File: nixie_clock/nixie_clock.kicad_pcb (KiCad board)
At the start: 2 copper layers, 147.3 x 92.7 mm, 52 parts, among them P1 CONN_01X04, P10 CONN_01X03, P11 CONN_01X02, P12 CONN_01X03, P13 CONN_01X02, P2 CONN_01X03, P3 CONN_01X02, P4 CONN_01X03, P5 CONN_01X02, P6 CONN_01X03, P7 CONN_01X02, P8 CONN_01X03, P9 CONN_01X02, U1 4518, U10 K155ID1, U11 IN-12, U12 4518, U13 4011, U14 K155ID1, U15 IN-12, U16 K155ID1, U17 IN-12, U2 4011, U3 K155ID1, U4 IN-12, U5 K155ID1, U6 IN-12, U7 4518, U8 K155ID1, U9 IN-12

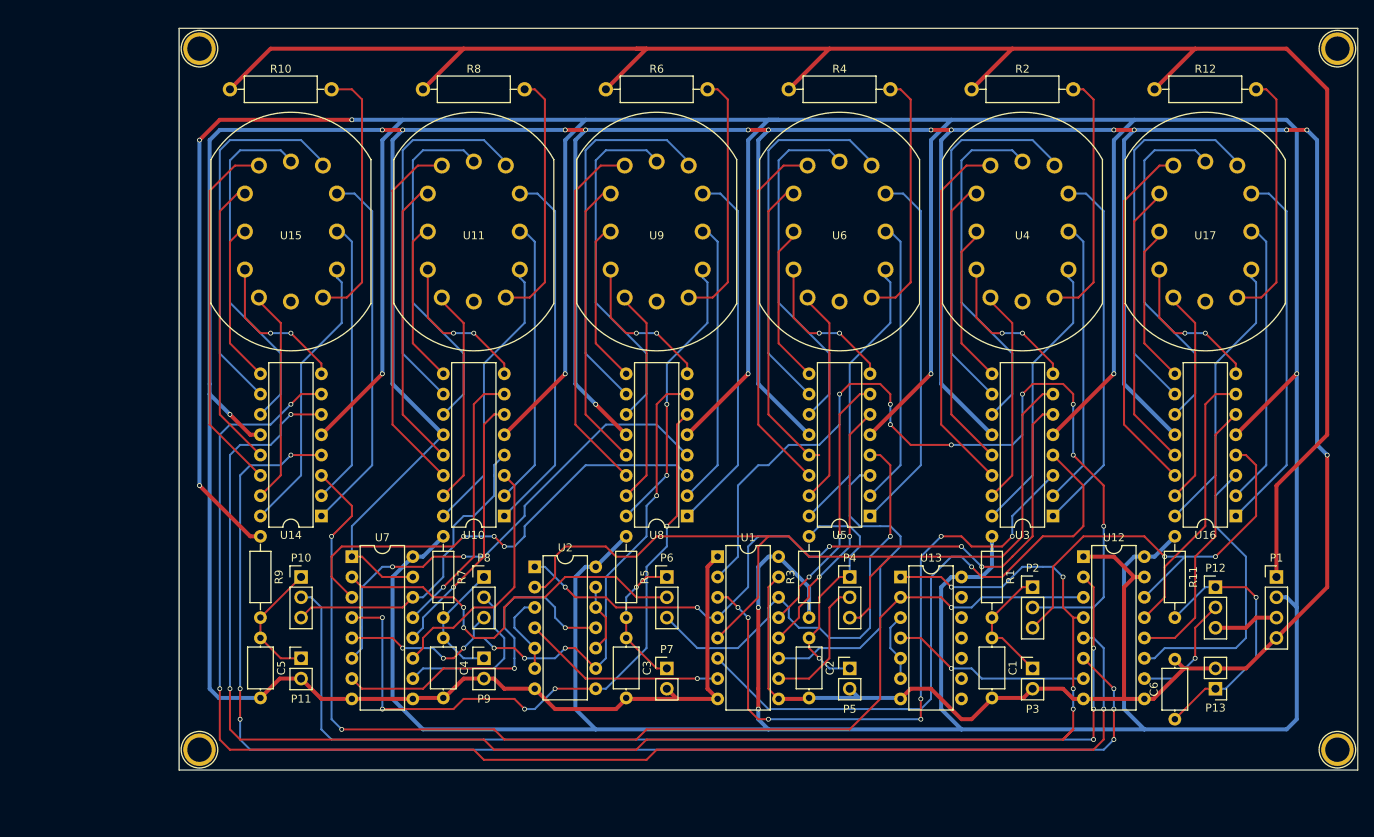
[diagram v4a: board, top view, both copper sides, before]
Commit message: Overhaul of clock board. Fixed hour digits, added more noise immunity, reduced height
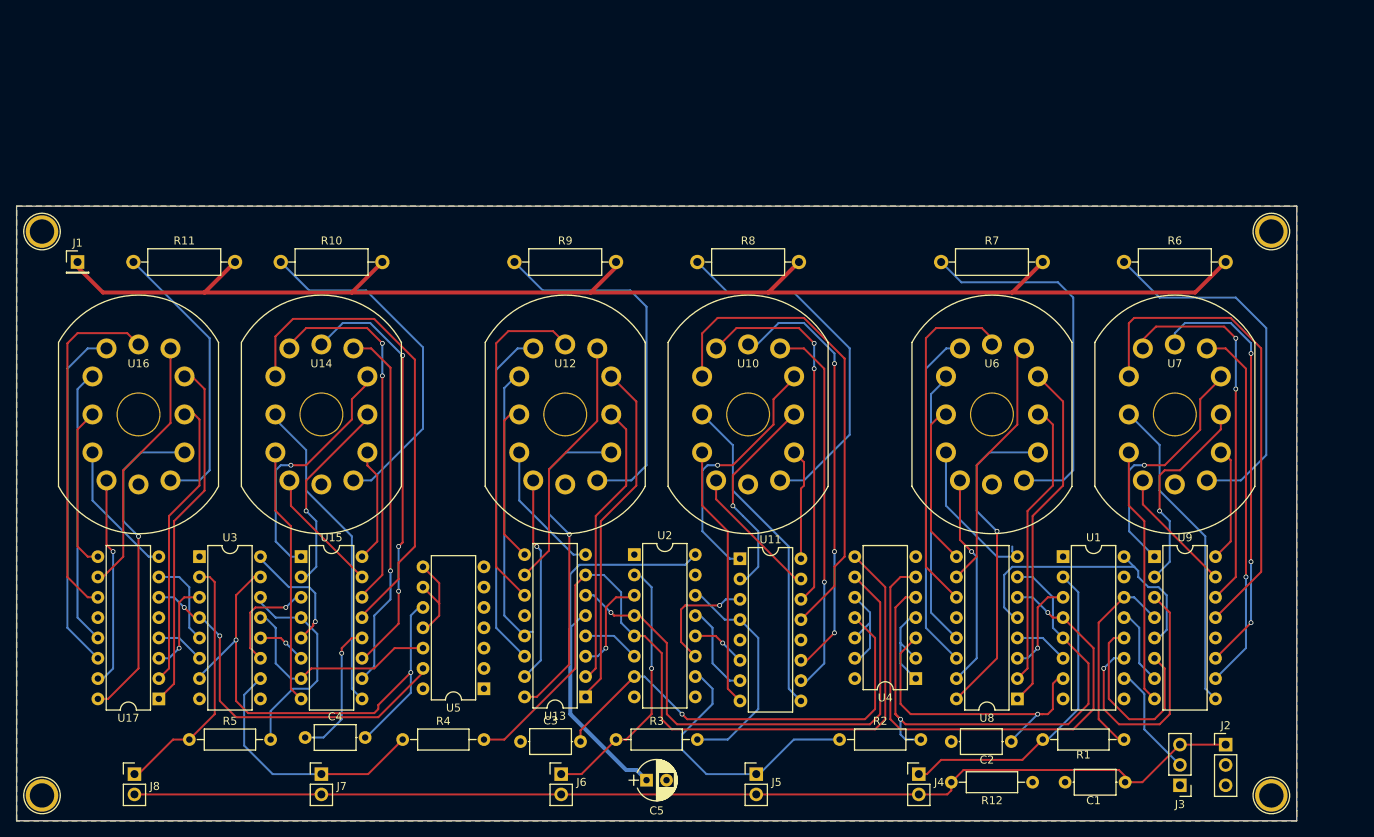
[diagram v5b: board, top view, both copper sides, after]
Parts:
- removed C6: 0.1uF, Capacitors_THT:C_Axial_L5.1mm_D3.1mm_P7.50mm_Horizontal
- removed P1: CONN_01X04, Pin_Headers:Pin_Header_Straight_1x04_Pitch2.54mm
- removed P10, P12, P2, P4, P6, P8: CONN_01X03, Pin_Headers:Pin_Header_Straight_1x03_Pitch2.54mm
- removed P11, P13, P3, P5, P7, P9: CONN_01X02, Pin_Headers:Pin_Header_Straight_1x02_Pitch2.54mm
- removed the REF** at (78.7, 24.1)
- removed the REF** at (221.0, 24.1)
- removed the REF** at (221.0, 111.8)
- removed the REF** at (78.7, 111.8)
- added J1: CONN_01X01, Pin_Headers:Pin_Header_Straight_1x01_Pitch2.54mm, F.Cu at (63.5, 50.8)
- added J2: CONN_01X03, Pin_Headers:Pin_Header_Straight_1x03_Pitch2.54mm, F.Cu at (207.0, 111.1)
- added J3: CONN_01X03, Pin_Headers:Pin_Header_Straight_1x03_Pitch2.54mm, F.Cu at (201.3, 116.2)
- added J4: CONN_01X02, Pin_Headers:Pin_Header_Straight_1x02_Pitch2.54mm, F.Cu at (168.7, 114.8)
- added J5: CONN_01X02, Pin_Headers:Pin_Header_Straight_1x02_Pitch2.54mm, F.Cu at (148.3, 114.8)
- added J6: CONN_01X02, Pin_Headers:Pin_Header_Straight_1x02_Pitch2.54mm, F.Cu at (124.0, 114.8)
- added J7: CONN_01X02, Pin_Headers:Pin_Header_Straight_1x02_Pitch2.54mm, F.Cu at (94.0, 114.8)
- added J8: CONN_01X02, Pin_Headers:Pin_Header_Straight_1x02_Pitch2.54mm, F.Cu at (70.6, 114.8)
- added REF**: 1pin, Connectors:1pin, F.Cu at (59.1, 47.0)
- added REF**: 1pin, Connectors:1pin, F.Cu at (212.7, 47.0)
- added REF**: 1pin, Connectors:1pin, F.Cu at (59.1, 117.5)
- added REF**: 1pin, Connectors:1pin, F.Cu at (212.7, 117.5)
- C5: value 0.1uF -> 10uF; footprint Capacitors_THT:C_Axial_L5.1mm_D3.1mm_P7.50mm_Horizontal -> Capacitors_THT:CP_Radial_D5.0mm_P2.50mm
- R11, R7, R9: value 1K -> 33K; footprint Resistors_THT:R_Axial_DIN0207_L6.3mm_D2.5mm_P10.16mm_Horizontal -> hv:R_Axial_DIN0309_L9.0mm_D3.2mm_P12.70mm_Horizontal_Thick
- R12: value 33K -> 4.7K; footprint hv:R_Axial_DIN0309_L9.0mm_D3.2mm_P12.70mm_Horizontal_Thick -> Resistors_THT:R_Axial_DIN0207_L6.3mm_D2.5mm_P10.16mm_Horizontal
- R2, R4: value 33K -> 1K; footprint hv:R_Axial_DIN0309_L9.0mm_D3.2mm_P12.70mm_Horizontal_Thick -> Resistors_THT:R_Axial_DIN0207_L6.3mm_D2.5mm_P10.16mm_Horizontal
- U10, U14, U16: value K155ID1 -> IN-12; footprint Housings_DIP:DIP-16_W7.62mm -> hv:IN12
- U11, U15, U17, U9: value IN-12 -> K155ID1; footprint hv:IN12 -> Housings_DIP:DIP-16_W7.62mm
- U12, U7: value 4518 -> IN-12; footprint Housings_DIP:DIP-16_W7.62mm -> hv:IN12
- U13: value 4011 -> K155ID1; footprint Housings_DIP:DIP-14_W7.62mm -> Housings_DIP:DIP-16_W7.62mm
- U2: value 4011 -> 4518; footprint Housings_DIP:DIP-14_W7.62mm -> Housings_DIP:DIP-16_W7.62mm
- U3: value K155ID1 -> 4518
- U4: value IN-12 -> 4011; footprint hv:IN12 -> Housings_DIP:DIP-14_W7.62mm
- U5: value K155ID1 -> 4011; footprint Housings_DIP:DIP-16_W7.62mm -> Housings_DIP:DIP-14_W7.62mm
- moved U17 143.3 mm to (73.7, 105.4), turned to 180 degrees
- moved U16 137.7 mm to (71.1, 69.8), turned to 0 degrees
- moved R11 134.6 mm to (70.5, 50.8), turned to 0 degrees
- moved U3 106.8 mm to (78.7, 87.6), turned to 0 degrees
- moved U7 104.4 mm to (200.7, 69.8)
- moved R4 101.6 mm to (104.1, 110.5), turned to 0 degrees
- moved R12 94.6 mm to (172.7, 115.8), turned to 0 degrees
- moved R2 86.4 mm to (158.8, 110.5), turned to 0 degrees
- moved U9 74.3 mm to (198.1, 87.6)
- moved R7 71.1 mm to (171.4, 50.8), turned to 0 degrees
- moved U12 67.2 mm to (124.5, 69.8)
- moved R5 60.2 mm to (77.5, 110.5), turned to 0 degrees
- moved U4 57.4 mm to (168.3, 102.9), turned to 180 degrees
- moved R6 56.4 mm to (194.3, 50.8), turned to 0 degrees
- moved U5 52.9 mm to (114.3, 104.1)
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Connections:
- C1 pad 1: Net-(C1-Pad1) -> GND
- C1 pad 2: GND -> Net-(C1-Pad2)
- C2 pad 1: Net-(C2-Pad1) -> GND
- C2 pad 2: GND -> Net-(C2-Pad2)
- C3 pad 1: Net-(C3-Pad1) -> GND
- C3 pad 2: GND -> Net-(C3-Pad2)
- C4 pad 1: Net-(C4-Pad1) -> GND
- C4 pad 2: GND -> Net-(C4-Pad2)
- C5 pad 1: Net-(C5-Pad1) -> +5V
- R1 pad 1: +5V -> Net-(J4-Pad1)
- R1 pad 2: Net-(C1-Pad1) -> /1second/8s
- R10 pad 2: +220V -> +240V
- R11 pad 1: +5V -> Net-(R11-Pad1)
- R11 pad 2: Net-(C6-Pad1) -> +240V
- R12 pad 1: Net-(R12-Pad1) -> Net-(C1-Pad2)
- R12 pad 2: +220V -> GND
- R2 pad 1: Net-(R2-Pad1) -> Net-(J5-Pad1)
- R2 pad 2: +220V -> /10second/4s
- R3 pad 1: +5V -> Net-(J6-Pad1)
- R3 pad 2: Net-(C2-Pad1) -> /1minute/8s
- R4 pad 1: Net-(R4-Pad1) -> Net-(J7-Pad1)
- R4 pad 2: +220V -> /10minute/4s
- R5 pad 1: +5V -> Net-(J8-Pad1)
- R5 pad 2: Net-(C3-Pad1) -> /1hour/8s
- R6 pad 2: +220V -> +240V
- R7 pad 1: +5V -> Net-(R7-Pad1)
- R7 pad 2: Net-(C4-Pad1) -> +240V
- R8 pad 2: +220V -> +240V
- R9 pad 1: +5V -> Net-(R9-Pad1)
- R9 pad 2: Net-(C5-Pad1) -> +240V
- U1 pad 11: Net-(U1-Pad11) -> /1second/1s
- U1 pad 12: Net-(U1-Pad12) -> /1second/2s
- U1 pad 13: Net-(U1-Pad13) -> /1second/4s
- U1 pad 14: /10minute/CLK_IN -> /1second/8s
- U1 pad 2: Net-(P2-Pad2) -> Net-(J4-Pad1)
- U1 pad 3: Net-(U1-Pad3) -> /10second/1s
- U1 pad 4: Net-(U1-Pad4) -> /10second/2s
- U1 pad 5: /1minute/CLK_IN -> /10second/4s
- U1 pad 6: Net-(U1-Pad6) -> /10second/8s
- U1 pad 7: Net-(U1-Pad7) -> Net-(C2-Pad2)
- U10 pad 1: Net-(U10-Pad1) -> Net-(R8-Pad1)
- U10 pad 12: GND -> Net-(U10-Pad12)
- U10 pad 13: Net-(U10-Pad13) -> (no net)
- U10 pad 4: /10hour/CLK_IN -> Net-(U10-Pad4)
- U10 pad 5: +5V -> Net-(U10-Pad5)
- U11 pad 1: Net-(R8-Pad1) -> Net-(U10-Pad4)
- U11 pad 10: Net-(U10-Pad8) -> Net-(U10-Pad5)
- U11 pad 11: Net-(U10-Pad15) -> Net-(U10-Pad6)
- U11 pad 12: Net-(U11-Pad12) -> GND
- U11 pad 2: Net-(U10-Pad16) -> Net-(U10-Pad3)
- U11 pad 3: Net-(U10-Pad2) -> /1minute/1s
- U11 pad 4: Net-(U10-Pad1) -> /1minute/8s
- U11 pad 5: Net-(U10-Pad10) -> +5V
- U11 pad 6: Net-(U10-Pad11) -> /1minute/2s
- U11 pad 7: Net-(U10-Pad14) -> /1minute/4s
- U11 pad 8: Net-(U10-Pad13) -> Net-(U10-Pad10)
- U12 pad 1: GND -> Net-(R9-Pad1)
- U12 pad 10: Net-(P12-Pad2) -> Net-(U12-Pad10)
- U12 pad 13: Net-(U12-Pad13) -> (no net)
- U12 pad 2: Net-(P10-Pad2) -> Net-(U12-Pad2)
- U12 pad 8: GND -> Net-(U12-Pad8)
- U12 pad 9: GND -> Net-(U12-Pad9)
- U13 pad 10: (no net) -> Net-(U12-Pad5)
- U13 pad 11: (no net) -> Net-(U12-Pad6)
- U13 pad 12: (no net) -> GND
- U13 pad 13: (no net) -> Net-(U12-Pad8)
- U13 pad 14: +5V -> Net-(U12-Pad7)
- U13 pad 3: Net-(U13-Pad3) -> /10minute/1s
- U13 pad 4: Net-(U12-Pad7) -> /10minute/8s
- U13 pad 5: Net-(U13-Pad3) -> +5V
- U13 pad 6: Net-(U13-Pad3) -> /10minute/2s
- U13 pad 7: GND -> /10minute/4s
- U13 pad 8: (no net) -> Net-(U12-Pad10)
- U13 pad 9: (no net) -> Net-(U12-Pad9)
- U14 pad 1: Net-(U14-Pad1) -> Net-(R10-Pad1)
- U14 pad 12: GND -> Net-(U14-Pad12)
- U14 pad 13: Net-(U14-Pad13) -> (no net)
- U14 pad 3: Net-(U12-Pad3) -> Net-(U14-Pad3)
- U14 pad 4: Net-(U12-Pad6) -> Net-(U14-Pad4)
- U14 pad 5: +5V -> Net-(U14-Pad5)
- U14 pad 6: Net-(U12-Pad4) -> Net-(U14-Pad6)
- U14 pad 7: Net-(U12-Pad5) -> Net-(U14-Pad7)
- U15 pad 1: Net-(R10-Pad1) -> Net-(U14-Pad4)
- U15 pad 10: Net-(U14-Pad8) -> Net-(U14-Pad5)
- U15 pad 11: Net-(U14-Pad15) -> Net-(U14-Pad6)
- U15 pad 12: Net-(U15-Pad12) -> GND
- U15 pad 2: Net-(U14-Pad16) -> Net-(U14-Pad3)
- U15 pad 3: Net-(U14-Pad2) -> /1hour/1s
- U15 pad 4: Net-(U14-Pad1) -> /1hour/8s
- U15 pad 5: Net-(U14-Pad10) -> +5V
- U15 pad 6: Net-(U14-Pad11) -> /1hour/2s
- U15 pad 7: Net-(U14-Pad14) -> /1hour/4s
- U15 pad 8: Net-(U14-Pad13) -> Net-(U14-Pad10)
- U16 pad 1: Net-(U16-Pad1) -> Net-(R11-Pad1)
- U16 pad 12: GND -> Net-(U16-Pad12)
- U16 pad 13: Net-(U16-Pad13) -> (no net)
- U16 pad 3: Net-(U12-Pad11) -> Net-(U16-Pad3)
- U16 pad 4: /10second/CLK_IN -> Net-(U16-Pad4)
- U16 pad 5: +5V -> Net-(U16-Pad5)
- U16 pad 6: Net-(U12-Pad12) -> Net-(U16-Pad6)
- U16 pad 7: Net-(U12-Pad13) -> Net-(U16-Pad7)
- U17 pad 1: Net-(R12-Pad1) -> Net-(U16-Pad4)
- U17 pad 10: Net-(U16-Pad8) -> Net-(U16-Pad5)
- U17 pad 11: Net-(U16-Pad15) -> Net-(U16-Pad6)
- U17 pad 12: Net-(U17-Pad12) -> GND
- U17 pad 2: Net-(U16-Pad16) -> Net-(U16-Pad3)
- U17 pad 3: Net-(U16-Pad2) -> /10hour/1s
- U17 pad 4: Net-(U16-Pad1) -> /10hour/8s
- U17 pad 5: Net-(U16-Pad10) -> +5V
- U17 pad 6: Net-(U16-Pad11) -> /10hour/2s
- U17 pad 7: Net-(U16-Pad14) -> /10hour/4s
- U17 pad 8: Net-(U16-Pad13) -> Net-(U16-Pad10)
- U2 pad 1: Net-(U1-Pad4) -> GND
- U2 pad 10: Net-(U2-Pad10) -> Net-(J5-Pad1)
- U2 pad 11: Net-(U2-Pad11) -> /1minute/1s
- U2 pad 12: Net-(U2-Pad10) -> /1minute/2s
- U2 pad 13: Net-(U2-Pad10) -> /1minute/4s
- U2 pad 14: +5V -> /1minute/8s
- U2 pad 2: /1minute/CLK_IN -> Net-(J6-Pad1)
- U2 pad 3: Net-(U2-Pad3) -> /10minute/1s
- U2 pad 4: Net-(U1-Pad7) -> /10minute/2s
- U2 pad 5: Net-(U2-Pad3) -> /10minute/4s
- U2 pad 6: Net-(U2-Pad3) -> /10minute/8s
- U2 pad 7: GND -> Net-(C3-Pad2)
- U2 pad 8: Net-(U2-Pad8) -> GND
- U2 pad 9: /1hour/CLK_IN -> GND
- U3 pad 1: Net-(U3-Pad1) -> GND
- U3 pad 10: Net-(U3-Pad10) -> Net-(J7-Pad1)
- U3 pad 11: Net-(U3-Pad11) -> /1hour/1s
- U3 pad 12: GND -> /1hour/2s
- U3 pad 13: Net-(U3-Pad13) -> /1hour/4s
- U3 pad 14: Net-(U3-Pad14) -> /1hour/8s
- U3 pad 15: Net-(U3-Pad15) -> Net-(C4-Pad2)
- U3 pad 16: Net-(U3-Pad16) -> +5V
- U3 pad 2: Net-(U3-Pad2) -> Net-(J8-Pad1)
- U3 pad 3: Net-(U1-Pad3) -> /10hour/1s
- U3 pad 4: Net-(U1-Pad6) -> /10hour/2s
- U3 pad 5: +5V -> /10hour/4s
- U3 pad 6: Net-(U1-Pad4) -> /10hour/8s
- U3 pad 7: /1minute/CLK_IN -> Net-(C4-Pad2)
- U3 pad 8: Net-(U3-Pad8) -> GND
- U3 pad 9: Net-(U3-Pad9) -> GND
- U4 pad 1: Net-(R2-Pad1) -> Net-(U4-Pad1)
- U4 pad 10: Net-(U3-Pad8) -> Net-(U4-Pad10)
- U4 pad 11: Net-(U3-Pad15) -> Net-(C3-Pad2)
- U4 pad 12: Net-(U4-Pad12) -> Net-(U4-Pad10)
- U4 pad 2: Net-(U3-Pad16) -> Net-(U4-Pad1)
- U4 pad 3: Net-(U3-Pad2) -> Net-(C2-Pad2)
- U4 pad 4: Net-(U3-Pad1) -> Net-(U4-Pad1)
- U4 pad 5: Net-(U3-Pad10) -> /10second/4s
- U4 pad 6: Net-(U3-Pad11) -> /10second/2s
- U4 pad 7: Net-(U3-Pad14) -> GND
- U4 pad 8: Net-(U3-Pad13) -> /10minute/4s
- U4 pad 9: Net-(U3-Pad9) -> /10minute/2s
- U5 pad 1: Net-(U5-Pad1) -> (no net)
- U5 pad 10: Net-(U5-Pad10) -> Net-(C4-Pad2)
- U5 pad 12: GND -> /1hour/4s
- U5 pad 13: Net-(U5-Pad13) -> /10hour/2s
- U5 pad 14: Net-(U5-Pad14) -> +5V
- U5 pad 2: Net-(U5-Pad2) -> (no net)
- U5 pad 3: Net-(U1-Pad11) -> (no net)
- U5 pad 4: /10minute/CLK_IN -> (no net)
- U5 pad 5: +5V -> (no net)
- U5 pad 6: Net-(U1-Pad12) -> (no net)
- U5 pad 7: Net-(U1-Pad13) -> GND
- U5 pad 8: Net-(U5-Pad8) -> Net-(U5-Pad11)
- U5 pad 9: Net-(U5-Pad9) -> Net-(U5-Pad11)
- U6 pad 1: Net-(R4-Pad1) -> Net-(R7-Pad1)
- U6 pad 10: Net-(U5-Pad8) -> Net-(U6-Pad10)
- U6 pad 11: Net-(U5-Pad15) -> Net-(U6-Pad11)
- U6 pad 2: Net-(U5-Pad16) -> Net-(U6-Pad2)
- U6 pad 3: Net-(U5-Pad2) -> Net-(U6-Pad3)
- U6 pad 4: Net-(U5-Pad1) -> Net-(U6-Pad4)
- U6 pad 5: Net-(U5-Pad10) -> Net-(U6-Pad5)
- U6 pad 6: Net-(U5-Pad11) -> Net-(U6-Pad6)
- U6 pad 7: Net-(U5-Pad14) -> Net-(U6-Pad7)
- U6 pad 8: Net-(U5-Pad13) -> Net-(U6-Pad8)
- U6 pad 9: Net-(U5-Pad9) -> Net-(U6-Pad9)
- U7 pad 1: GND -> Net-(R6-Pad1)
- U7 pad 10: Net-(P8-Pad2) -> Net-(U7-Pad10)
- U7 pad 11: Net-(U10-Pad3) -> Net-(U7-Pad11)
- U7 pad 12: Net-(U10-Pad6) -> Net-(U7-Pad12)
- U7 pad 13: Net-(U10-Pad7) -> (no net)
- U7 pad 2: Net-(P6-Pad2) -> Net-(U7-Pad2)
- U7 pad 4: Net-(U2-Pad8) -> Net-(U7-Pad4)
- U7 pad 5: /1hour/CLK_IN -> Net-(U7-Pad5)
- U7 pad 7: Net-(U2-Pad11) -> Net-(U7-Pad7)
- U7 pad 8: GND -> Net-(U7-Pad8)
- U7 pad 9: GND -> Net-(U7-Pad9)
- U8 pad 1: Net-(U8-Pad1) -> Net-(U6-Pad4)
- U8 pad 10: Net-(U8-Pad10) -> Net-(U6-Pad5)
- U8 pad 11: Net-(U8-Pad11) -> Net-(U6-Pad6)
- U8 pad 13: Net-(U8-Pad13) -> Net-(U6-Pad8)
- U8 pad 14: Net-(U8-Pad14) -> Net-(U6-Pad7)
- U8 pad 15: Net-(U8-Pad15) -> Net-(U6-Pad11)
- U8 pad 16: Net-(U8-Pad16) -> Net-(U6-Pad2)
- U8 pad 2: Net-(U8-Pad2) -> Net-(U6-Pad3)
- U8 pad 3: Net-(U7-Pad3) -> /10second/1s
- U8 pad 4: Net-(U7-Pad6) -> /10second/8s
- U8 pad 6: Net-(U2-Pad8) -> /10second/2s
- U8 pad 7: /1hour/CLK_IN -> /10second/4s
- U8 pad 8: Net-(U8-Pad8) -> Net-(U6-Pad10)
- U8 pad 9: Net-(U8-Pad9) -> Net-(U6-Pad9)
- U9 pad 1: Net-(R6-Pad1) -> Net-(U7-Pad4)
- U9 pad 10: Net-(U8-Pad8) -> Net-(U7-Pad5)
- U9 pad 11: Net-(U8-Pad15) -> Net-(U7-Pad6)
- U9 pad 12: Net-(U9-Pad12) -> GND
- U9 pad 2: Net-(U8-Pad16) -> Net-(U7-Pad3)
- U9 pad 3: Net-(U8-Pad2) -> /1second/1s
- U9 pad 4: Net-(U8-Pad1) -> /1second/8s
- U9 pad 5: Net-(U8-Pad10) -> +5V
- U9 pad 6: Net-(U8-Pad11) -> /1second/2s
- U9 pad 7: Net-(U8-Pad14) -> /1second/4s
- U9 pad 8: Net-(U8-Pad13) -> Net-(U7-Pad10)
- U9 pad 9: Net-(U8-Pad9) -> Net-(U7-Pad9)
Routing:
- net GND: track 721.1 -> 17.5 mm, vias 15 -> 1
- net +5V: track 758.7 -> 101.8 mm, vias 11 -> 1
- net +220V: track 242.1 -> 0.00 mm
- net +240V: track 0.00 -> 173.7 mm
- net Net-(U12-Pad4): track 202.9 -> 44.0 mm, vias 6 -> 0
- net Net-(U12-Pad5): track 180.0 -> 32.1 mm, vias 3 -> 0
- net Net-(C1-Pad2): track 0.00 -> 140.8 mm
- net Net-(P10-Pad2): track 136.2 -> 0.00 mm, vias 3 -> 0
- net Net-(U12-Pad6): track 166.2 -> 43.0 mm, vias 6 -> 0
- net /1minute/CLK_IN: track 114.1 -> 0.00 mm
- net Net-(P2-Pad2): track 110.3 -> 0.00 mm, vias 8 -> 0
- net Net-(U12-Pad3): track 142.5 -> 36.3 mm, vias 3 -> 0
- net /10minute/4s: track 0.00 -> 102.3 mm
- net Net-(U1-Pad4): track 93.3 -> 0.00 mm, vias 5 -> 0
- net Net-(U2-Pad8): track 83.8 -> 0.00 mm, vias 5 -> 0
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- added copper zone on F.Cu, net +5V
- added copper zone on B.Cu, net GND
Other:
- board size 147.3 x 92.7 mm -> 160 x 76.8 mm
- net class High Voltage added: clearance 1, trace_width 0.25, via_dia 0.6, via_drill 0.4
